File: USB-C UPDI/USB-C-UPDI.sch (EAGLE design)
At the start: 9 parts, among them IC1 FT232RL, J2 61300511121

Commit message: updates
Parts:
- added C1: 100nf, 01_SparkFun:CAP1206
- added R3, R4: 5.1k, 01_SparkFun:RESISTOR1206
- added R5, R6: 330, 01_SparkFun:RESISTOR1206
- added RX-LED, TX-LED: LED, eagle_fab:LED
- C10: value 1uf -> 4.7uf
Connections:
- new net N$1: C1.1, IC1.3V3OUT
- new net N$42: J1.CC2, R3.1
- new net N$43: IC1.CBUS1, R6.1
- new net N$44: IC1.CBUS0, R5.1
- new net N$45: R5.2, RX-LED.C
- new net N$46: R6.2, TX-LED.C
- net GND: now also C1.2, J1.SHLD, R3.2, R4.2
- net N$9: now also J1.CC1, R4.1; no longer C4.1, IC1.!RESET, IC1.3V3OUT, IC1.VCCIO
- net VCC: now also C4.1, IC1.VCCIO, RX-LED.A, TX-LED.A
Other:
- moved on the sheet: C10, C4, D1, J1, J2, R1, R2, S1

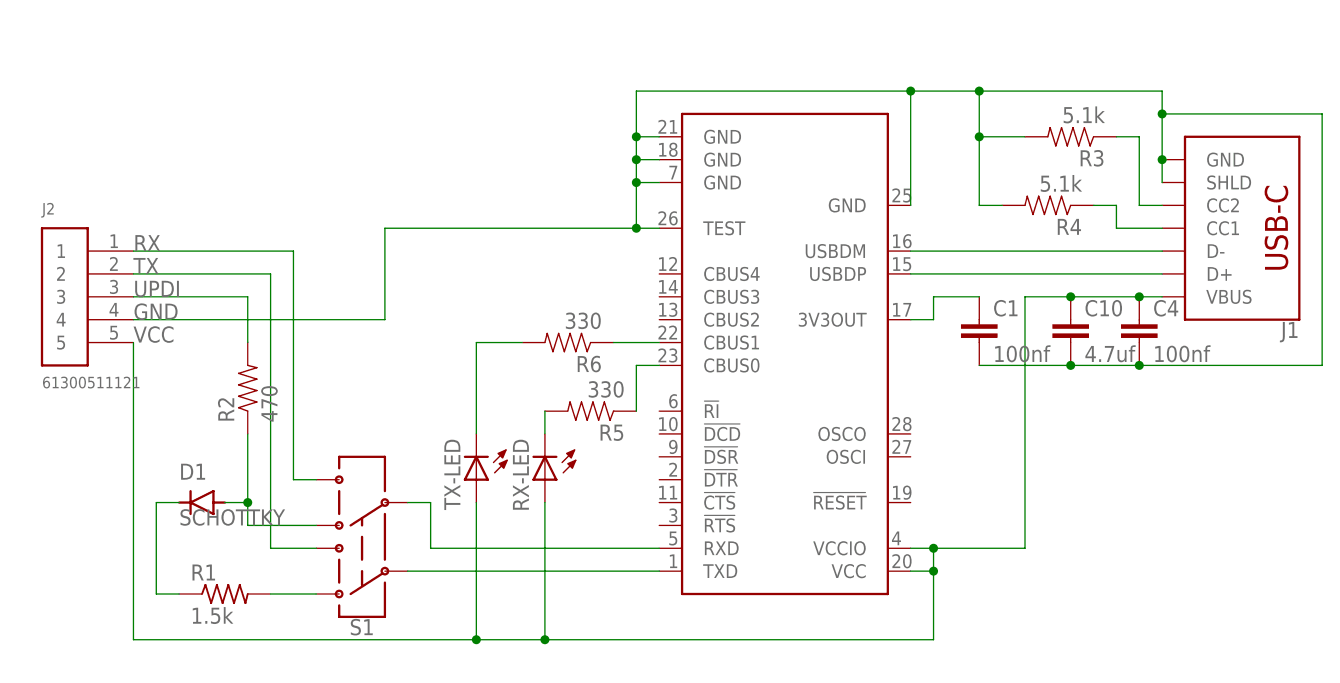
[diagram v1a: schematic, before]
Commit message: UPDI updates
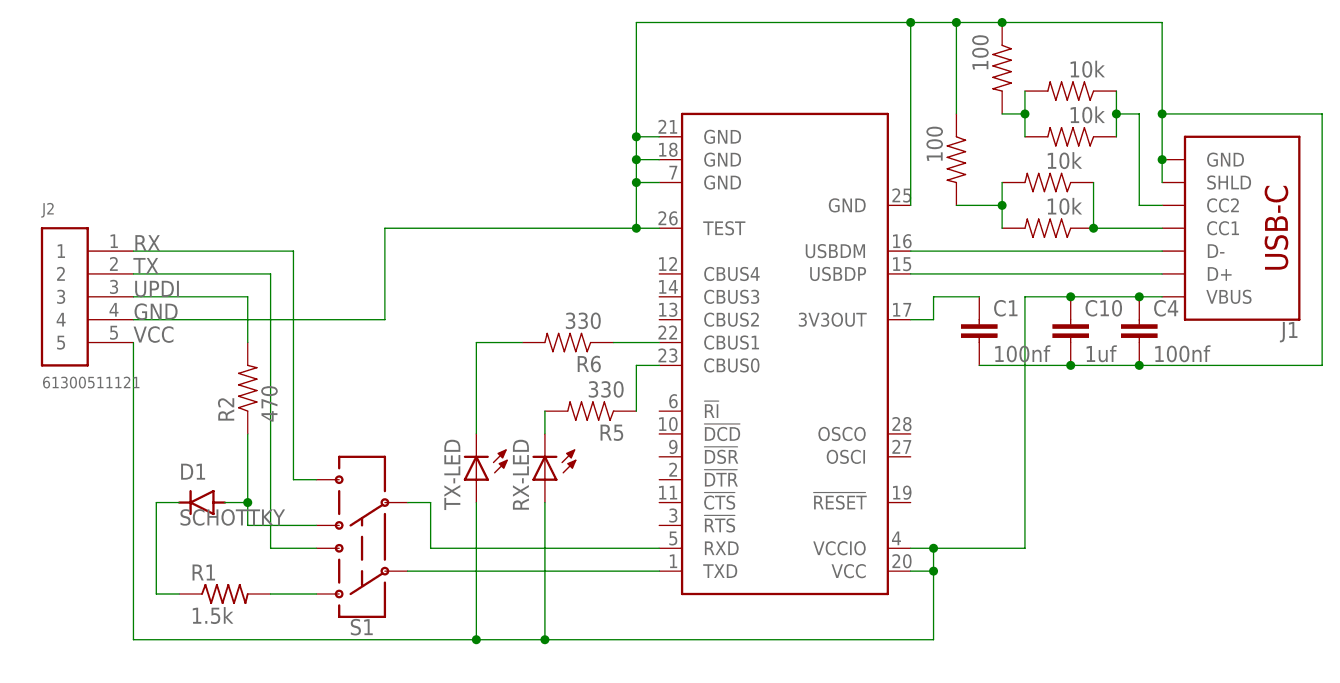
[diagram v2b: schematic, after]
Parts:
- added R10, R9: 100, 01_SparkFun:RESISTOR1206
- added R7, R8: 10k, 01_SparkFun:RESISTOR1206
- C10: value 4.7uf -> 1uf
- R3, R4: value 5.1k -> 10k
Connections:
- new net N$49: J1.CC2, R3.1, R7.1
- new net N$50: R10.2, R3.2, R7.2
- net GND: now also R10.1, R9.1; no longer R3.2, R4.2
- net N$42: now also R4.2, R8.2, R9.2; no longer J1.CC2, R3.1
- net N$9: now also R8.1
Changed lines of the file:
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@@
 <part name="J1" library="SparkFun-Connectors" deviceset="USB_C" device="_2-LAYER_PADS"/>
 <part name="C4" library="01_SparkFun" deviceset="CAP" device="1206" value="100nf"/>
-<part name="C10" library="01_SparkFun" deviceset="CAP" device="1206" value="4.7uf"/>
+<part name="C10" library="01_SparkFun" deviceset="CAP" device="1206" value="1uf"/>
 <part name="R2" library="01_SparkFun" deviceset="RESISTOR" device="1206" value="470"/>
 <part name="D1" library="eagle_fab" deviceset="DIODE_SCHOTTKY_CDBM1100-G" device="" value="SCHOTTKY"/>
@@
 <part name="R1" library="eagle_fab" deviceset="R" device="1206FAB" value="1.5k"/>
 <part name="C1" library="01_SparkFun" deviceset="CAP" device="1206" value="100nf"/>
-<part name="R3" library="01_SparkFun" deviceset="RESISTOR" device="1206" value="5.1k"/>
-<part name="R4" library="01_SparkFun" deviceset="RESISTOR" device="1206" value="5.1k"/>
+<part name="R3" library="01_SparkFun" deviceset="RESISTOR" device="1206" value="10k"/>
+<part name="R4" library="01_SparkFun" deviceset="RESISTOR" device="1206" value="10k"/>
 <part name="R5" library="01_SparkFun" deviceset="RESISTOR" device="1206" value="330"/>
 <part name="R6" library="01_SparkFun" deviceset="RESISTOR" device="1206" value="330"/>
 <part name="RX-LED" library="eagle_fab" deviceset="LED" device=""/>
 <part name="TX-LED" library="eagle_fab" deviceset="LED" device=""/>
+<part name="R7" library="01_SparkFun" deviceset="RESISTOR" device="1206" value="10k"/>
+<part name="R8" library="01_SparkFun" deviceset="RESISTOR" device="1206" value="10k"/>
+<part name="R9" library="01_SparkFun" deviceset="RESISTOR" device="1206" value="100"/>
+<part name="R10" library="01_SparkFun" deviceset="RESISTOR" device="1206" value="100"/>
 </parts>
 <sheets>
@@
 <attribute name="VALUE" x="108.204" y="33.401" size="1.778" layer="96"/>
 </instance>
-<instance part="R3" gate="G$1" x="116.84" y="58.42" smashed="yes" rot="R180">
-<attribute name="NAME" x="120.65" y="56.9214" size="1.778" layer="95" rot="R180"/>
-<attribute name="VALUE" x="120.65" y="61.722" size="1.778" layer="96" rot="R180"/>
-</instance>
-<instance part="R4" gate="G$1" x="114.3" y="50.8" smashed="yes" rot="R180">
-<attribute name="NAME" x="118.11" y="49.3014" size="1.778" layer="95" rot="R180"/>
-<attribute name="VALUE" x="118.11" y="54.102" size="1.778" layer="96" rot="R180"/>
+<instance part="R3" gate="G$1" x="116.84" y="63.5" smashed="yes" rot="R180">
+<attribute name="VALUE" x="120.65" y="66.802" size="1.778" layer="96" rot="R180"/>
+</instance>
+<instance part="R4" gate="G$1" x="114.3" y="48.26" smashed="yes" rot="R180">
+<attribute name="VALUE" x="118.11" y="51.562" size="1.778" layer="96" rot="R180"/>
 </instance>
 <instance part="R5" gate="G$1" x="63.5" y="27.94" smashed="yes" rot="R180">
@@
 <instance part="TX-LED" gate="G$1" x="50.8" y="22.86" smashed="yes" rot="R180">
 <attribute name="NAME" x="47.244" y="24.892" size="1.778" layer="95" rot="R270"/>
+</instance>
+<instance part="R7" gate="G$1" x="116.84" y="58.42" smashed="yes" rot="R180">
+<attribute name="VALUE" x="120.65" y="61.722" size="1.778" layer="96" rot="R180"/>
+</instance>
+<instance part="R8" gate="G$1" x="114.3" y="53.34" smashed="yes" rot="R180">
+<attribute name="VALUE" x="118.11" y="56.642" size="1.778" layer="96" rot="R180"/>
+</instance>
+<instance part="R9" gate="G$1" x="104.14" y="55.88" smashed="yes" rot="R270">
+<attribute name="VALUE" x="100.838" y="59.69" size="1.778" layer="96" rot="R270"/>
+</instance>
+<instance part="R10" gate="G$1" x="109.22" y="66.04" smashed="yes" rot="R270">
+<attribute name="VALUE" x="105.918" y="69.85" size="1.778" layer="96" rot="R270"/>
 </instance>
 </instances>
@@
 <pinref part="IC1" gate="1" pin="GND@2"/>
 <wire x1="68.58" y1="58.42" x2="71.12" y2="58.42" width="0.1524" layer="91"/>
-<wire x1="68.58" y1="58.42" x2="68.58" y2="63.5" width="0.1524" layer="91"/>
+<wire x1="68.58" y1="58.42" x2="68.58" y2="71.12" width="0.1524" layer="91"/>
 <junction x="68.58" y="58.42"/>
 <pinref part="IC1" gate="1" pin="GND@A"/>
-<wire x1="68.58" y1="63.5" x2="99.06" y2="63.5" width="0.1524" layer="91"/>
-<wire x1="99.06" y1="63.5" x2="99.06" y2="50.8" width="0.1524" layer="91"/>
-<wire x1="99.06" y1="63.5" x2="106.68" y2="63.5" width="0.1524" layer="91"/>
-<junction x="99.06" y="63.5"/>
+<wire x1="68.58" y1="71.12" x2="99.06" y2="71.12" width="0.1524" layer="91"/>
+<wire x1="99.06" y1="71.12" x2="99.06" y2="50.8" width="0.1524" layer="91"/>
+<junction x="99.06" y="71.12"/>
 <pinref part="J1" gate="J1" pin="GND"/>
-<wire x1="106.68" y1="63.5" x2="127" y2="63.5" width="0.1524" layer="91"/>
+<wire x1="99.06" y1="71.12" x2="104.14" y2="71.12" width="0.1524" layer="91"/>
+<wire x1="104.14" y1="71.12" x2="109.22" y2="71.12" width="0.1524" layer="91"/>
+<wire x1="109.22" y1="71.12" x2="127" y2="71.12" width="0.1524" layer="91"/>
 <wire x1="127" y1="55.88" x2="127" y2="60.96" width="0.1524" layer="91"/>
 <wire x1="127" y1="60.96" x2="144.78" y2="60.96" width="0.1524" layer="91"/>
@@
 <wire x1="124.46" y1="33.02" x2="116.84" y2="33.02" width="0.1524" layer="91"/>
 <junction x="124.46" y="33.02"/>
-<wire x1="127" y1="63.5" x2="127" y2="60.96" width="0.1524" layer="91"/>
+<wire x1="127" y1="71.12" x2="127" y2="60.96" width="0.1524" layer="91"/>
 <junction x="127" y="60.96"/>
 <wire x1="40.64" y1="48.26" x2="68.58" y2="48.26" width="0.1524" layer="91"/>
@@
 <wire x1="127" y1="53.34" x2="127" y2="55.88" width="0.1524" layer="91"/>
 <junction x="127" y="55.88"/>
-<junction x="106.68" y="63.5"/>
-<pinref part="R3" gate="G$1" pin="2"/>
-<wire x1="106.68" y1="58.42" x2="106.68" y2="63.5" width="0.1524" layer="91"/>
-<wire x1="111.76" y1="58.42" x2="106.68" y2="58.42" width="0.1524" layer="91"/>
-<wire x1="106.68" y1="58.42" x2="106.68" y2="50.8" width="0.1524" layer="91"/>
-<junction x="106.68" y="58.42"/>
-<pinref part="R4" gate="G$1" pin="2"/>
-<wire x1="106.68" y1="50.8" x2="109.22" y2="50.8" width="0.1524" layer="91"/>
+<pinref part="R10" gate="G$1" pin="1"/>
+<junction x="109.22" y="71.12"/>
+<pinref part="R9" gate="G$1" pin="1"/>
+<wire x1="104.14" y1="60.96" x2="104.14" y2="71.12" width="0.1524" layer="91"/>
+<junction x="104.14" y="71.12"/>
 </segment>
 </net>
@@
 </segment>
 </net>
-<net name="N$42" class="0">
-<segment>
-<pinref part="J1" gate="J1" pin="CC2"/>
-<wire x1="127" y1="50.8" x2="124.46" y2="50.8" width="0.1524" layer="91"/>
-<wire x1="124.46" y1="50.8" x2="124.46" y2="58.42" width="0.1524" layer="91"/>
-<pinref part="R3" gate="G$1" pin="1"/>
-<wire x1="124.46" y1="58.42" x2="121.92" y2="58.42" width="0.1524" layer="91"/>
-</segment>
-</net>
 <net name="N$9" class="0">
 <segment>
 <pinref part="R4" gate="G$1" pin="1"/>
-<wire x1="119.38" y1="50.8" x2="121.92" y2="50.8" width="0.1524" layer="91"/>
-<wire x1="121.92" y1="50.8" x2="121.92" y2="48.26" width="0.1524" layer="91"/>
 <pinref part="J1" gate="J1" pin="CC1"/>
-<wire x1="121.92" y1="48.26" x2="127" y2="48.26" width="0.1524" layer="91"/>
+<wire x1="119.38" y1="48.26" x2="127" y2="48.26" width="0.1524" layer="91"/>
+<pinref part="R8" gate="G$1" pin="1"/>
+<wire x1="119.38" y1="53.34" x2="119.38" y2="48.26" width="0.1524" layer="91"/>
+<junction x="119.38" y="48.26"/>
 </segment>
 </net>
@@
 </segment>
 </net>
+<net name="N$49" class="0">
+<segment>
+<pinref part="R3" gate="G$1" pin="1"/>
+<pinref part="R7" gate="G$1" pin="1"/>
+<wire x1="121.92" y1="63.5" x2="121.92" y2="60.96" width="0.1524" layer="91"/>
+<pinref part="J1" gate="J1" pin="CC2"/>
+<wire x1="121.92" y1="60.96" x2="121.92" y2="58.42" width="0.1524" layer="91"/>
+<wire x1="127" y1="50.8" x2="124.46" y2="50.8" width="0.1524" layer="91"/>
+<wire x1="124.46" y1="50.8" x2="124.46" y2="60.96" width="0.1524" layer="91"/>
+<wire x1="121.92" y1="60.96" x2="124.46" y2="60.96" width="0.1524" layer="91"/>
+<junction x="121.92" y="60.96"/>
+</segment>
+</net>
+<net name="N$42" class="0">
+<segment>
+<pinref part="R8" gate="G$1" pin="2"/>
+<pinref part="R4" gate="G$1" pin="2"/>
+<wire x1="109.22" y1="48.26" x2="109.22" y2="50.8" width="0.1524" layer="91"/>
+<wire x1="109.22" y1="50.8" x2="109.22" y2="53.34" width="0.1524" layer="91"/>
+<junction x="109.22" y="50.8"/>
+<wire x1="109.22" y1="50.8" x2="104.14" y2="50.8" width="0.1524" layer="91"/>
+<pinref part="R9" gate="G$1" pin="2"/>
+</segment>
+</net>
+<net name="N$50" class="0">
+<segment>
+<pinref part="R3" gate="G$1" pin="2"/>
+<pinref part="R7" gate="G$1" pin="2"/>
+<wire x1="111.76" y1="58.42" x2="111.76" y2="60.96" width="0.1524" layer="91"/>
+<wire x1="111.76" y1="60.96" x2="111.76" y2="63.5" width="0.1524" layer="91"/>
+<junction x="111.76" y="60.96"/>
+<wire x1="111.76" y1="60.96" x2="109.22" y2="60.96" width="0.1524" layer="91"/>
+<pinref part="R10" gate="G$1" pin="2"/>
+</segment>
+</net>

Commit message: updates
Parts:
- C1: value 100nf -> 1uf
- C10: value 1uf -> 10uf
- J1: device SparkFun-Connectors:USB_C_2-LAYER_PADS -> SparkFun-Connectors:USB_C_4-LAYER_PADS
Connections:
- net VCC: now also IC1.!RESET
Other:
- moved on the sheet: C10, C4

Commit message: Updates
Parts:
- C1: value 1uf -> 100nf
- R1: value 1.5k -> 1k
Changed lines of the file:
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@@
 <grid distance="0.1" unitdist="inch" unit="inch" style="lines" multiple="1" display="no" altdistance="0.01" altunitdist="inch" altunit="inch"/>
 <layers>
-<layer number="1" name="Top" color="4" fill="1" visible="yes" active="no"/>
-<layer number="2" name="Route2" color="16" fill="1" visible="yes" active="no"/>
-<layer number="3" name="Route3" color="17" fill="1" visible="yes" active="no"/>
-<layer number="4" name="Route4" color="18" fill="1" visible="yes" active="no"/>
-<layer number="5" name="Route5" color="19" fill="1" visible="yes" active="no"/>
-<layer number="6" name="Route6" color="25" fill="1" visible="yes" active="no"/>
-<layer number="7" name="Route7" color="26" fill="1" visible="yes" active="no"/>
-<layer number="8" name="Route8" color="27" fill="1" visible="yes" active="no"/>
-<layer number="9" name="Route9" color="28" fill="1" visible="yes" active="no"/>
-<layer number="10" name="Route10" color="29" fill="1" visible="yes" active="no"/>
-<layer number="11" name="Route11" color="30" fill="1" visible="yes" active="no"/>
-<layer number="12" name="Route12" color="20" fill="1" visible="yes" active="no"/>
-<layer number="13" name="Route13" color="21" fill="1" visible="yes" active="no"/>
-<layer number="14" name="Route14" color="22" fill="1" visible="yes" active="no"/>
-<layer number="15" name="Route15" color="23" fill="1" visible="yes" active="no"/>
-<layer number="16" name="Bottom" color="1" fill="1" visible="yes" active="no"/>
-<layer number="17" name="Pads" color="2" fill="1" visible="yes" active="no"/>
-<layer number="18" name="Vias" color="2" fill="1" visible="yes" active="no"/>
-<layer number="19" name="Unrouted" color="6" fill="1" visible="yes" active="no"/>
-<layer number="20" name="Dimension" color="24" fill="1" visible="yes" active="no"/>
-<layer number="21" name="tPlace" color="7" fill="1" visible="yes" active="no"/>
-<layer number="22" name="bPlace" color="7" fill="1" visible="yes" active="no"/>
-<layer number="23" name="tOrigins" color="15" fill="1" visible="yes" active="no"/>
-<layer number="24" name="bOrigins" color="15" fill="1" visible="yes" active="no"/>
-<layer number="25" name="tNames" color="7" fill="1" visible="yes" active="no"/>
-<layer number="26" name="bNames" color="7" fill="1" visible="yes" active="no"/>
-<layer number="27" name="tValues" color="7" fill="1" visible="yes" active="no"/>
-<layer number="28" name="bValues" color="7" fill="1" visible="yes" active="no"/>
+<layer number="1" name="Top" color="4" fill="1" visible="no" active="no"/>
+<layer number="2" name="Route2" color="16" fill="1" visible="no" active="no"/>
+<layer number="3" name="Route3" color="17" fill="1" visible="no" active="no"/>
+<layer number="4" name="Route4" color="18" fill="1" visible="no" active="no"/>
+<layer number="5" name="Route5" color="19" fill="1" visible="no" active="no"/>
+<layer number="6" name="Route6" color="25" fill="1" visible="no" active="no"/>
+<layer number="7" name="Route7" color="26" fill="1" visible="no" active="no"/>
+<layer number="8" name="Route8" color="27" fill="1" visible="no" active="no"/>
+<layer number="9" name="Route9" color="28" fill="1" visible="no" active="no"/>
+<layer number="10" name="Route10" color="29" fill="1" visible="no" active="no"/>
+<layer number="11" name="Route11" color="30" fill="1" visible="no" active="no"/>
+<layer number="12" name="Route12" color="20" fill="1" visible="no" active="no"/>
+<layer number="13" name="Route13" color="21" fill="1" visible="no" active="no"/>
+<layer number="14" name="Route14" color="22" fill="1" visible="no" active="no"/>
+<layer number="15" name="Route15" color="23" fill="1" visible="no" active="no"/>
+<layer number="16" name="Bottom" color="1" fill="1" visible="no" active="no"/>
+<layer number="17" name="Pads" color="2" fill="1" visible="no" active="no"/>
+<layer number="18" name="Vias" color="2" fill="1" visible="no" active="no"/>
+<layer number="19" name="Unrouted" color="6" fill="1" visible="no" active="no"/>
+<layer number="20" name="Dimension" color="24" fill="1" visible="no" active="no"/>
+<layer number="21" name="tPlace" color="7" fill="1" visible="no" active="no"/>
+<layer number="22" name="bPlace" color="7" fill="1" visible="no" active="no"/>
+<layer number="23" name="tOrigins" color="15" fill="1" visible="no" active="no"/>
+<layer number="24" name="bOrigins" color="15" fill="1" visible="no" active="no"/>
+<layer number="25" name="tNames" color="7" fill="1" visible="no" active="no"/>
+<layer number="26" name="bNames" color="7" fill="1" visible="no" active="no"/>
+<layer number="27" name="tValues" color="7" fill="1" visible="no" active="no"/>
+<layer number="28" name="bValues" color="7" fill="1" visible="no" active="no"/>
 <layer number="29" name="tStop" color="7" fill="3" visible="no" active="no"/>
 <layer number="30" name="bStop" color="7" fill="6" visible="no" active="no"/>
@@
 <layer number="35" name="tGlue" color="7" fill="4" visible="no" active="no"/>
 <layer number="36" name="bGlue" color="7" fill="5" visible="no" active="no"/>
-<layer number="37" name="tTest" color="7" fill="1" visible="yes" active="no"/>
-<layer number="38" name="bTest" color="7" fill="1" visible="yes" active="no"/>
+<layer number="37" name="tTest" color="7" fill="1" visible="no" active="no"/>
+<layer number="38" name="bTest" color="7" fill="1" visible="no" active="no"/>
 <layer number="39" name="tKeepout" color="4" fill="11" visible="no" active="no"/>
 <layer number="40" name="bKeepout" color="1" fill="11" visible="no" active="no"/>
@@
 <layer number="44" name="Drills" color="7" fill="1" visible="no" active="no"/>
 <layer number="45" name="Holes" color="7" fill="1" visible="no" active="no"/>
-<layer number="46" name="Milling" color="3" fill="1" visible="yes" active="no"/>
-<layer number="47" name="Measures" color="7" fill="1" visible="yes" active="no"/>
-<layer number="48" name="Document" color="7" fill="1" visible="yes" active="no"/>
-<layer number="49" name="Reference" color="7" fill="1" visible="yes" active="no"/>
-<layer number="50" name="dxf" color="7" fill="1" visible="yes" active="no"/>
-<layer number="51" name="tDocu" color="7" fill="1" visible="yes" active="no"/>
-<layer number="52" name="bDocu" color="7" fill="1" visible="yes" active="no"/>
-<layer number="53" name="tGND_GNDA" color="7" fill="9" visible="yes" active="no"/>
-<layer number="54" name="bGND_GNDA" color="1" fill="9" visible="yes" active="no"/>
-<layer number="56" name="wert" color="7" fill="1" visible="yes" active="no"/>
-<layer number="57" name="tCAD" color="7" fill="1" visible="yes" active="no"/>
-<layer number="59" name="tCarbon" color="7" fill="1" visible="yes" active="no"/>
-<layer number="60" name="bCarbon" color="7" fill="1" visible="yes" active="no"/>
+<layer number="46" name="Milling" color="3" fill="1" visible="no" active="no"/>
+<layer number="47" name="Measures" color="7" fill="1" visible="no" active="no"/>
+<layer number="48" name="Document" color="7" fill="1" visible="no" active="no"/>
+<layer number="49" name="Reference" color="7" fill="1" visible="no" active="no"/>
+<layer number="50" name="dxf" color="7" fill="1" visible="no" active="no"/>
+<layer number="51" name="tDocu" color="7" fill="1" visible="no" active="no"/>
+<layer number="52" name="bDocu" color="7" fill="1" visible="no" active="no"/>
+<layer number="53" name="tGND_GNDA" color="7" fill="9" visible="no" active="no"/>
+<layer number="54" name="bGND_GNDA" color="1" fill="9" visible="no" active="no"/>
+<layer number="56" name="wert" color="7" fill="1" visible="no" active="no"/>
+<layer number="57" name="tCAD" color="7" fill="1" visible="no" active="no"/>
+<layer number="59" name="tCarbon" color="7" fill="1" visible="no" active="no"/>
+<layer number="60" name="bCarbon" color="7" fill="1" visible="no" active="no"/>
 <layer number="88" name="SimResults" color="9" fill="1" visible="yes" active="yes"/>
 <layer number="89" name="SimProbes" color="9" fill="1" visible="yes" active="yes"/>
@@
 <part name="J2" library="Headers" library_urn="urn:adsk.eagle:library:11687645" deviceset="61300511121" device="" package3d_urn="urn:adsk.eagle:package:11390687/2"/>
 <part name="S1" library="SparkFun-Switches" deviceset="SWITCH-DPDT" device="-SMD-AYZ0202"/>
-<part name="R1" library="eagle_fab" deviceset="R" device="1206FAB" value="1.5k"/>
-<part name="C1" library="01_SparkFun" deviceset="CAP" device="1206" value="1uf"/>
+<part name="R1" library="eagle_fab" deviceset="R" device="1206FAB" value="1k"/>
+<part name="C1" library="01_SparkFun" deviceset="CAP" device="1206" value="100nf"/>
 <part name="R3" library="01_SparkFun" deviceset="RESISTOR" device="1206" value="10k"/>
 <part name="R4" library="01_SparkFun" deviceset="RESISTOR" device="1206" value="10k"/>
